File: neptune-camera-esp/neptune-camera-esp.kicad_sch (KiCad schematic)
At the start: 27 parts, among them J1 Conn_02x10_Odd_Even, J2 Conn_02x10_Odd_Even, J5 Programmersocket, SW1 EN_Button, SW2 BOOT_Button, U1 ESP32-S3-WROOM-1, U2 TLV74315, U3 TLV74328, U4 AP2112K-3.3

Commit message: kondi érték hiba javitasa
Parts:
- C22: value 22uF -> 100nF

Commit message: megyek ebédelni :)
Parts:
- added R10, R7, R8, R9: 22, Resistor_SMD:R_0402_1005Metric, symbol Device:R_Small
- U1: footprint neptune-camera-esp-footprints:ESP32-S3-WROOM-1 -> neptune-camera-esp-footprints:ESP32-S3-WROOM-1U
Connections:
- net +3.3V: no longer R5.2, R6.1
- net D2: now also R7.2; no longer U1.18 (IO10)
- net D3: now also R9.2; no longer U1.16 (IO46)
- net D4: now also R10.2; no longer U1.15 (IO3)
- net D5: now also R8.2; no longer U1.17 (IO9)
- net D6: no longer U1.19 (IO11)
- net D7: no longer U1.21 (IO13)
- net D8: no longer U1.22 (IO14)
- net D9: no longer U1.23 (IO21)
- net HSYNC: no longer U1.24 (IO47)
- net I2C_OBC_SCL: no longer U1.8 (IO15)
- net I2C_OBC_SDA: no longer U1.7 (IO7)
- net LTE_PWRKEY: no longer U1.34 (IO41)
- net LTE_RESET: no longer U1.35 (IO42)
- net OV5640_SCL: no longer R6.2, U1.31 (IO38)
- net OV5640_SDA: no longer R5.1, U1.32 (IO39)
- net PCLK: no longer U1.20 (IO12)
- net VSYNC: no longer U1.25 (IO48)
- net at U1.33 (IO40): now also R9.1
- new net: R10.1, U1.34 (IO41)
- new net: R7.1, U1.31 (IO38)
- new net: R8.1, U1.32 (IO39)
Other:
- moved on the sheet: R5, R6

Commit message: finom volt az ebéd, megyek haza
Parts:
- removed R10, R7, R8, R9: 22, Resistor_SMD:R_0402_1005Metric, symbol Device:R_Small
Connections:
- net +3.3V: now also R5.1, R6.2
- net D2: now also U1.31 (IO38)
- net D3: now also U1.33 (IO40)
- net D4: now also U1.34 (IO41)
- net D5: now also U1.32 (IO39)
- net D6: now also U1.26 (IO45)
- net D7: now also U1.24 (IO47)
- net D8: now also U1.23 (IO21)
- net D9: now also U1.21 (IO13)
- net HSYNC: now also U1.20 (IO12)
- net OV5640_SCL: now also R6.1, U1.12 (IO8)
- net OV5640_SDA: now also R5.2, U1.7 (IO7)
- net PCLK: now also U1.22 (IO14), U1.25 (IO48)
- net VSYNC: now also U1.18 (IO10)
- net CAM_PWDN: now reaches U1.17 (IO9)
- net CAM_RESET: now reaches U1.19 (IO11)
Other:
- sheet Camera(OV5640) ports: added CameraPWDN, CameraReset, XCLK; removed none
- moved on the sheet: R5, R6

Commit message: már nincs sok :)
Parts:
- added C20, C26: 1uF, Capacitor_SMD:C_0603_1608Metric, symbol Device:C_Small
- added U5: AP2112K-3.3, neptune-camera-esp-footprints:SOT-23-5, symbol Regulator_Linear:AP2112K-3.3
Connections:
- net +3.3V: no longer C22.2, C23.2, R3.1, R5.1, R6.2, U1.2 (3V3)
- net GND: now also C20.1, C26.2, U5.2 (GND)
- net I2C_OBC_SCL: now also U1.38 (IO2)
- net I2C_OBC_SDA: now also U1.39 (IO1)
- net LTE_PWRKEY: now also U1.10 (IO17)
- net LTE_RESET: now also U1.9 (IO16)
- net OV5640_SCL: now also U1.16 (IO46); no longer U1.12 (IO8)
- net OV5640_SDA: now also U1.15 (IO3); no longer U1.7 (IO7)
- net PCLK: no longer U1.22 (IO14)
- net VCC: now also C20.2, U5.1 (VIN), U5.3 (EN)
- new net +3.3VA: C22.2, C23.2, C26.1, R3.1, R5.1, R6.2, U1.2 (3V3), U5.5 (VOUT)
- new net XCLK: U1.22 (IO14)
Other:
- moved on the sheet: R5

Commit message: final
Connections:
- net D2: now also U1.32 (IO39); no longer U1.31 (IO38)
- net D3: now also U1.34 (IO41); no longer U1.33 (IO40)
- net D4: now also U1.35 (IO42); no longer U1.34 (IO41)
- net D5: now also U1.33 (IO40); no longer U1.32 (IO39)
- net D6: now also U1.31 (IO38); no longer U1.26 (IO45)
- net OV5640_SCL: now also U1.12 (IO8); no longer U1.16 (IO46)
- net OV5640_SDA: now also U1.11 (IO18); no longer U1.15 (IO3)

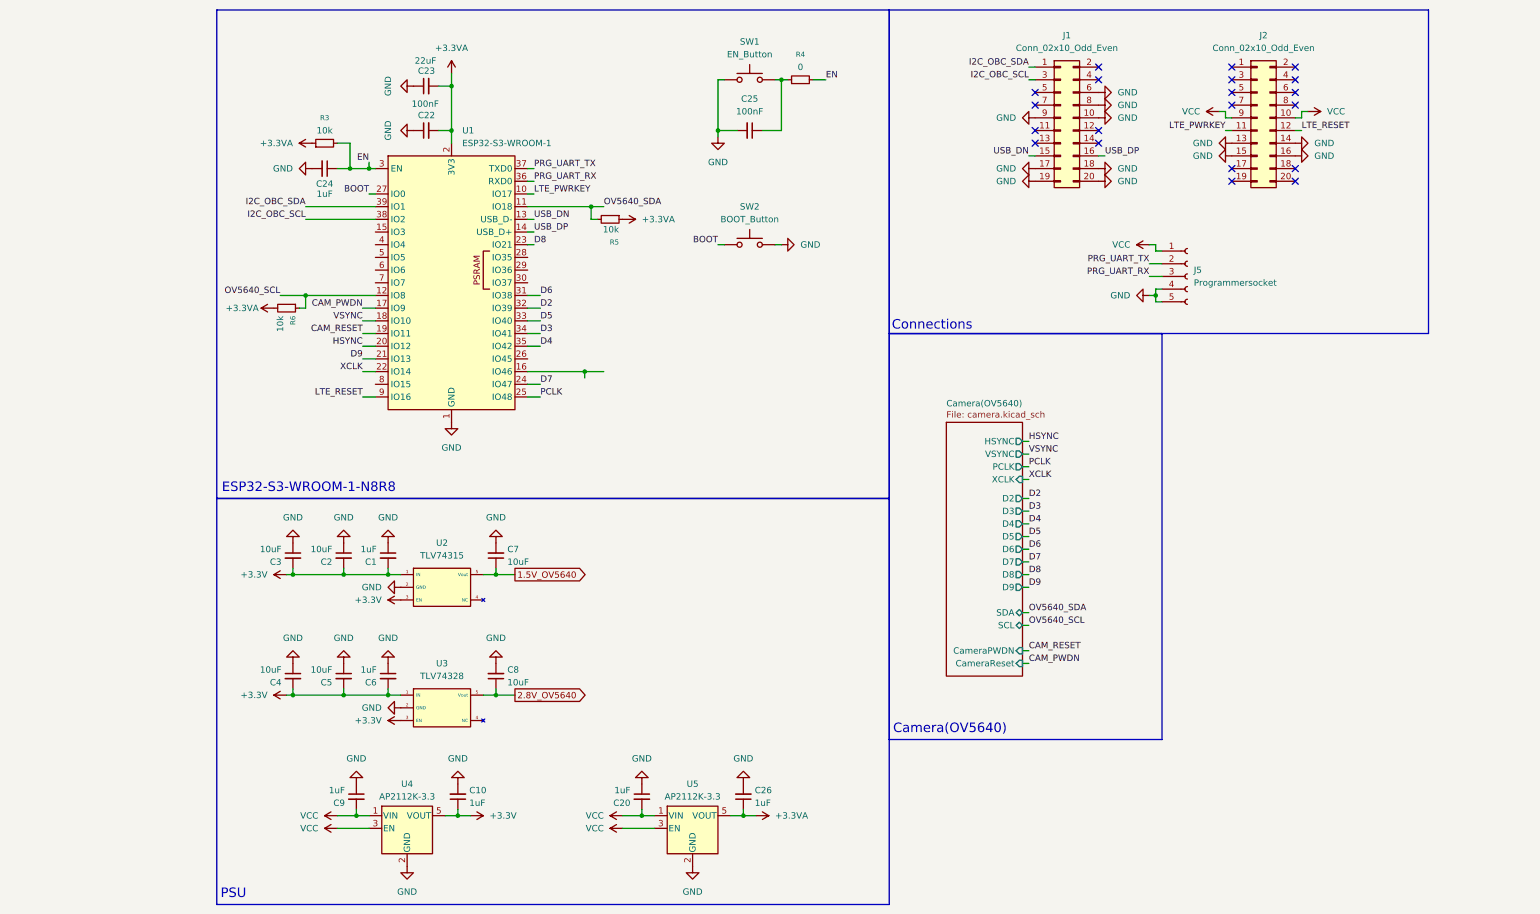
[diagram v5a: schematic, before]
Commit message: sd card added
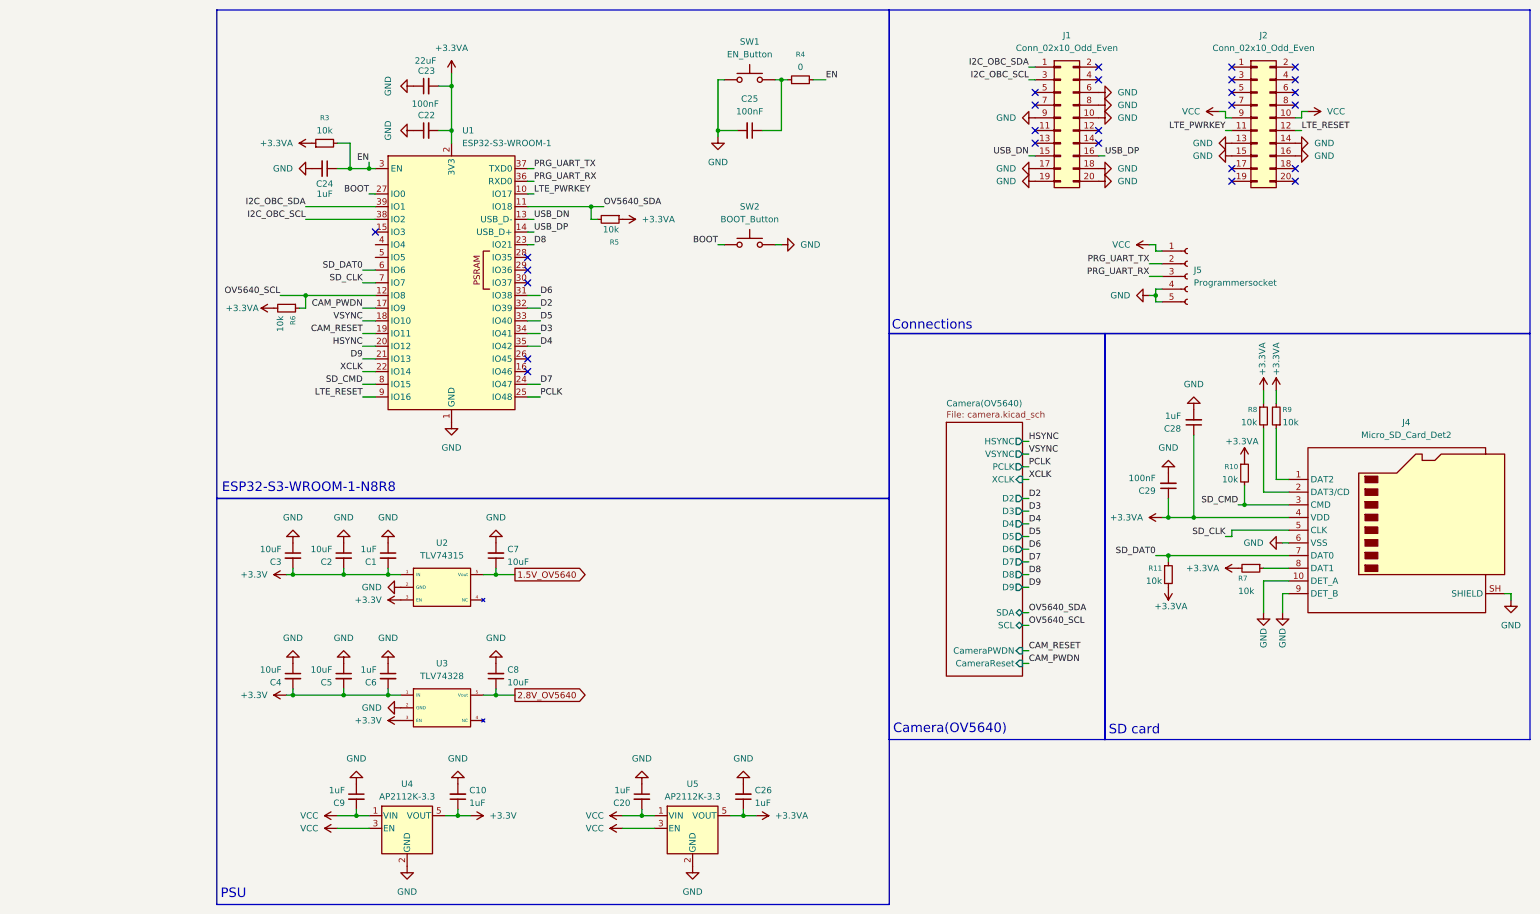
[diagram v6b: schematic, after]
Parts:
- added C28: 1uF, Capacitor_SMD:C_0603_1608Metric, symbol Device:C_Small
- added C29: 100nF, Capacitor_SMD:C_0402_1005Metric, symbol Device:C_Small
- added J4: Micro_SD_Card_Det2, Connector_Card:microSD_HC_Hirose_DM3D-SF, symbol Connector:Micro_SD_Card_Det2
- added R10, R11, R7, R8, R9: 10k, Resistor_SMD:R_0402_1005Metric, symbol Device:R_Small
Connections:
- net +3.3VA: now also C28.1, C29.1, J4.4 (VDD), R10.1, R11.2, R7.2, R8.1, R9.2
- net GND: now also C28.2, C29.2, J4.10 (DET_A), J4.6 (VSS), J4.9 (DET_B), J4.SH (SHIELD)
- net SD_DAT0: now reaches U1.6 (IO6)
- net SD_DAT0: now also J4.7 (DAT0), R11.1
- net SD_CLK: now reaches U1.7 (IO7)
- net SD_CLK: now also J4.5 (CLK)
- net SD_CMD: now reaches U1.8 (IO15)
- net SD_CMD: now also J4.3 (CMD), R10.2
- new net: J4.1 (DAT2), R9.1
- new net: J4.2 (DAT3/CD), R8.2
- new net: J4.8 (DAT1), R7.1
- no-connect marks 20 -> 26
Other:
- note added: "SD card"
